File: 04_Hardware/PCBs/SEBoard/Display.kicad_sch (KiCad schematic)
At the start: 35 parts, among them IC3 PCA9306DCTT, IC4 TXS0102DCUR, J14 FH12S-30S-0.5SH_55_, J15 FH12-8S-0.5SH_55_, U1 SC200EEMNA-E53-UGNDA, U9 AP5724WG-7

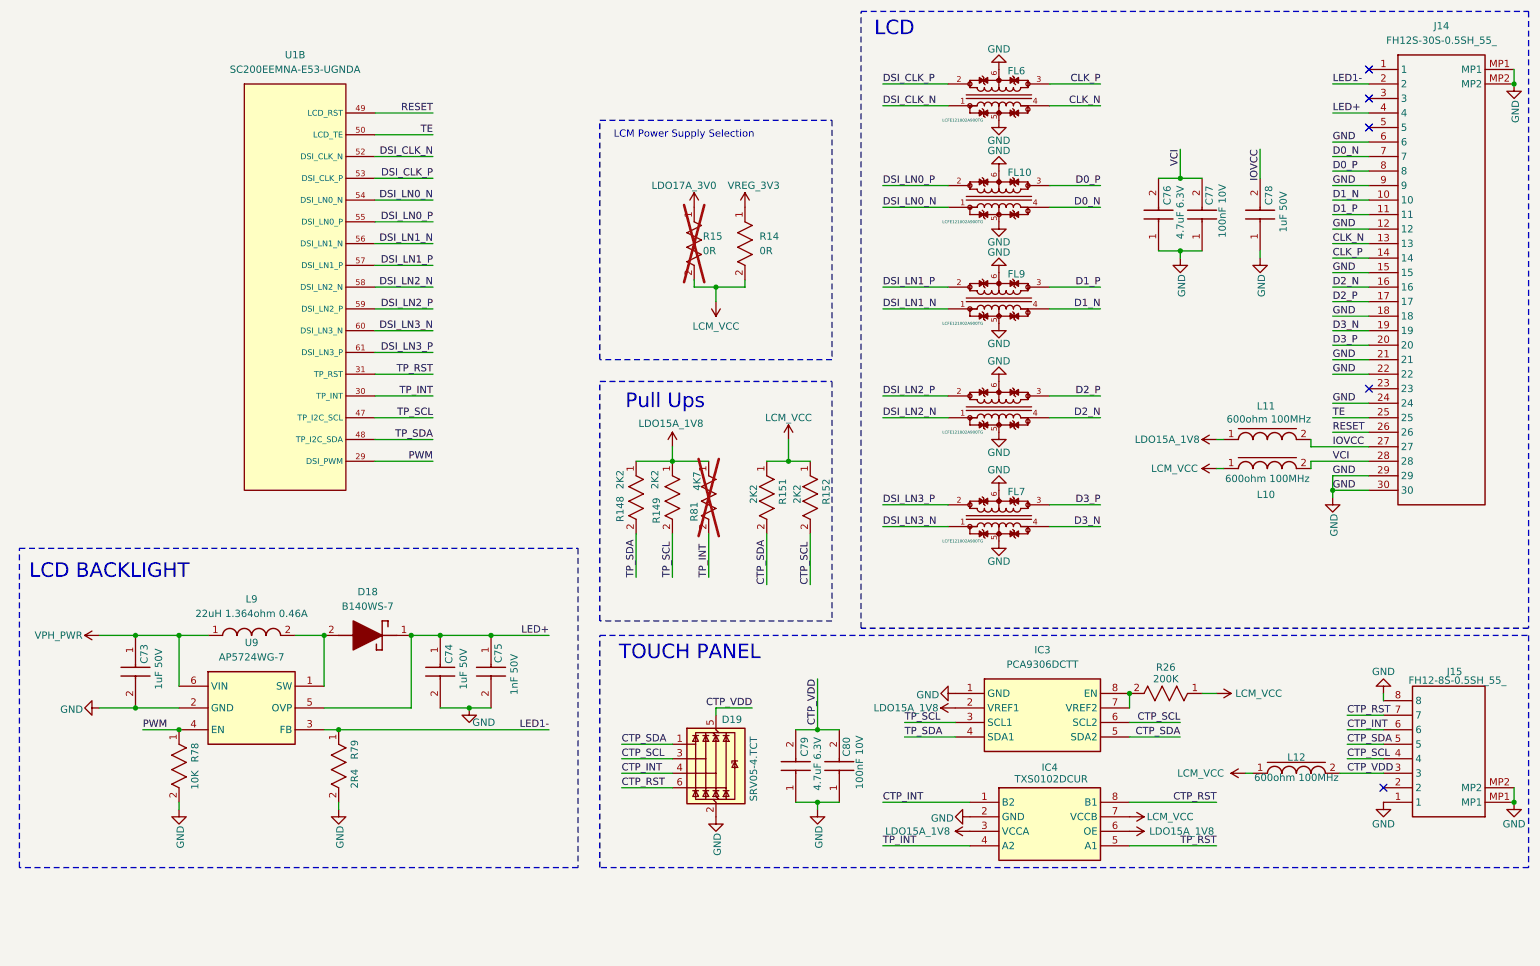
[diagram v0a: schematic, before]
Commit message: feat(schematic): add SE250B4 symbol to schematic (unchecked)
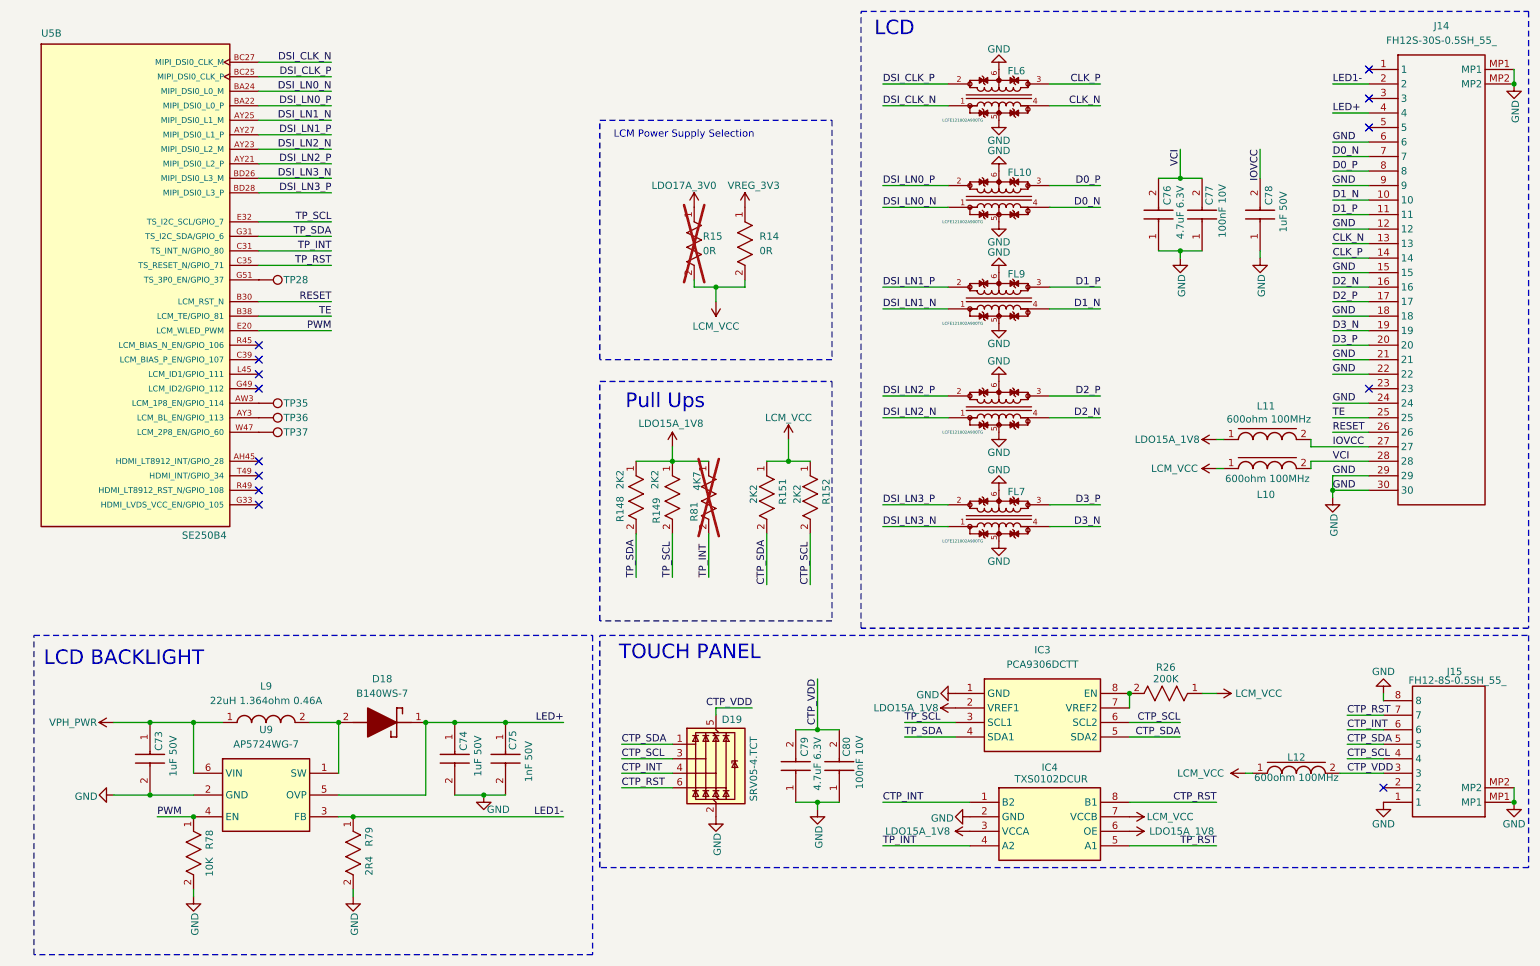
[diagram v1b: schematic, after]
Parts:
- removed U1: SC200EEMNA-E53-UGNDA, SEBoard:SC200E_SC206E, symbol SEBoard:SC200E
- added TP28, TP35, TP36, TP37: Sens_M, TestPoint:TestPoint_Pad_D1.0mm, symbol SEBoard:TestPoint
- added U5: SE250B4, 000MCLib:XCVR_SE250B4-NA, symbol 000MCLib:SE250B4
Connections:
- net DSI_CLK_N: now also U5.BC27 (MIPI_DSI0_CLK_M)
- net DSI_CLK_P: now also U5.BC25 (MIPI_DSI0_CLK_P)
- net DSI_LN0_N: now also U5.BA24 (MIPI_DSI0_L0_M)
- net DSI_LN0_P: now also U5.BA22 (MIPI_DSI0_L0_P)
- net DSI_LN1_N: now also U5.AY25 (MIPI_DSI0_L1_M)
- net DSI_LN1_P: now also U5.AY27 (MIPI_DSI0_L1_P)
- net DSI_LN2_N: now also U5.AY23 (MIPI_DSI0_L2_M)
- net DSI_LN2_P: now also U5.AY21 (MIPI_DSI0_L2_P)
- net DSI_LN3_N: now also U5.BD26 (MIPI_DSI0_L3_M)
- net DSI_LN3_P: now also U5.BD28 (MIPI_DSI0_L3_P)
- net PWM: now also U5.E20 (LCM_WLED_PWM)
- net RESET: now also U5.B30 (LCM_RST_N)
- net TE: now also U5.B38 (LCM_TE/GPIO_81)
- net TP_INT: now also U5.C31 (TS_INT_N/GPIO_80)
- net TP_RST: now also U5.C35 (TS_RESET_N/GPIO_71)
- net TP_SCL: now also U5.E32 (TS_I2C_SCL/GPIO_7)
- net TP_SDA: now also U5.G31 (TS_I2C_SDA/GPIO_6)
- new net: TP35.1, U5.AW3 (LCM_1P8_EN/GPIO_114)
- new net: TP36.1, U5.AY3 (LCM_BL_EN/GPIO_113)
- new net: TP28.1, U5.G51 (TS_3P0_EN/GPIO_37)
- new net: TP37.1, U5.W47 (LCM_2P8_EN/GPIO_60)
- no-connect marks 5 -> 13
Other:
- moved on the sheet: C73, C74, C75, D18, L9, R78, R79, U9

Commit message: feat: Updated schematic layout and moved new components to Layout
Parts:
- C73, C74, C78: footprint SEBoard:CAPC1005X55N -> 000MCLib:CAPC1005X55N; symbol SEBoard:GRM155R61H105KE05D -> 000MCLib:GRM155R61H105KE05D
- C75: footprint SEBoard:CAPC1005X55N -> 000MCLib:CAPC1005X55N; symbol SEBoard:GRM1555C1H102JA01D -> 000MCLib:GRM1555C1H102JA01D
- C76, C79: footprint SEBoard:CAPC1005X55N -> 000MCLib:CAPC1005X55N; symbol SEBoard:GRM155R60J475ME47D -> 000MCLib:GRM155R60J475ME47D
- C77, C80: footprint SEBoard:CAPC1005X55N -> 000MCLib:CAPC1005X55N; symbol SEBoard:GRM155R71A104KA01D -> 000MCLib:GRM155R71A104KA01D
- D18: footprint SEBoard:SOD2513X120N -> 000MCLib:SOD2513X120N; symbol SEBoard:B140WS-7 -> 000MCLib:B140WS-7
- D19: footprint SEBoard:SOT95P280X145-6N -> 000MCLib:SOT95P280X145-6N; symbol SEBoard:SRV05-4.TCT -> 000MCLib:SRV05-4.TCT
- FL10, FL6, FL7, FL8, FL9: footprint SEBoard:LCFE121002A900TG -> 000MCLib:LCFE121002A900TG; symbol SEBoard:LCFE121002A900TG -> 000MCLib:LCFE121002A900TG
- IC3: footprint SOP65P400X130-8N -> 000MCLib:SOP65P400X130-8N; symbol SEBoard:PCA9306DCTT -> 000MCLib:PCA9306DCTT
- IC4: footprint SEBoard:SOP50P310X90-8N -> 000MCLib:SOP50P310X90-8N; symbol SEBoard:TXS0102DCUR -> 000MCLib:TXS0102DCUR
- J14: footprint SEBoard:FH12S30S05SH55 -> 000MCLib:FH12S30S05SH55; symbol SEBoard:FH12S-30S-0.5SH_55_ -> 000MCLib:FH12S-30S-0.5SH_55_
- J15: footprint SEBoard:FH128S05SH55 -> 000MCLib:FH128S05SH55; symbol SEBoard:FH12-8S-0.5SH_55_ -> 000MCLib:FH12-8S-0.5SH_55_
- L10, L11, L12: footprint SEBoard:0402 -> 000MCLib:0402; symbol SEBoard:7427927291 -> 000MCLib:7427927291
- L9: footprint SEBoard:VLS2520 -> 000MCLib:VLS2520; symbol SEBoard:VLS252010CX-220M-1 -> 000MCLib:VLS252010CX-220M-1
- R14, R15: footprint SEBoard:RESC2012X50N -> 000MCLib:RESC2012X50N; symbol SEBoard:CRCW08050000Z0EA -> 000MCLib:CRCW08050000Z0EA
- R148, R149, R151, R152: footprint SEBoard:RC0402N_YAG -> 000MCLib:RC0402N_YAG; symbol SEBoard:RC0402JR-072K2L -> 000MCLib:RC0402JR-072K2L
- R26: footprint SEBoard:RC0402N_YAG -> 000MCLib:RC0402N_YAG; symbol SEBoard:RC0402FR-07200KL -> 000MCLib:RC0402FR-07200KL
- R78: footprint SEBoard:RC0402N_YAG -> 000MCLib:RC0402N_YAG; symbol SEBoard:RC0402JR-0710KL -> 000MCLib:RC0402JR-0710KL
- R79: footprint SEBoard:RC0402N_YAG -> 000MCLib:RC0402N_YAG; symbol SEBoard:RC0402JR-072R4L -> 000MCLib:RC0402JR-072R4L
- R81: footprint SEBoard:RC0402N_YAG -> 000MCLib:RC0402N_YAG; symbol SEBoard:RC0402JR-074K7L -> 000MCLib:RC0402JR-074K7L
- TP28, TP35, TP36, TP37: symbol SEBoard:TestPoint -> 000MCLib:TestPoint
- U9: footprint SEBoard:SOT95P285X140-6N -> 000MCLib:SOT95P285X140-6N; symbol SEBoard:AP5724WG-7 -> 000MCLib:AP5724WG-7

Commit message: feat: Updated schematic
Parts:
- added TP40: Sens_M, TestPoint:TestPoint_Pad_D1.0mm, symbol 000MCLib:TestPoint
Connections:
- net at U5.T49 (HDMI_INT/GPIO_34): now also TP40.1
- no-connect marks 13 -> 12
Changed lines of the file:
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@@
 	)
 	(no_connect
-		(at 57.15 96.52)
-	)
-	(no_connect
 		(at 254 151.13)
 	)
@@
 					(unit 1)
 				)
+			)
+		)
+	)
+	(symbol
+		(lib_id "000MCLib:TestPoint")
+		(at 57.15 96.52 270)
+		(unit 1)
+		(exclude_from_sim no)
+		(in_bom yes)
+		(on_board yes)
+		(dnp no)
+		(property "Reference" "TP40"
+			(at 61.468 96.52 90)
+			(effects
+				(font
+					(size 1.27 1.27)
+				)
+				(justify left)
+			)
+		)
+		(property "Value" "Sens_M"
+			(at 57.404 97.536 90)
+			(effects
+				(font
+					(size 0.635 0.635)
+				)
+				(hide yes)
+			)
+		)
+		(property "Footprint" "TestPoint:TestPoint_Pad_D1.0mm"
+			(at 57.15 101.6 0)
+			(effects
+				(font
+					(size 1.27 1.27)
+				)
+				(hide yes)
+			)
+		)
+		(property "Datasheet" "~"
+			(at 57.15 101.6 0)
+			(effects
+				(font
+					(size 1.27 1.27)
+				)
+				(hide yes)
+			)
+		)
+		(property "Description" "test point"
+			(at 57.15 96.52 0)
+			(effects
+				(font
+					(size 1.27 1.27)
+				)
+				(hide yes)
+			)
+		)
+		(pin "1"
+		)
+		(instances
+			(project "SEBoard"
+				(path "/38605b01-fdd9-41de-8a8b-501279ee3e8a/fd20983e-53dc-4079-9f17-527f4e836b8e"
+					(reference "TP40")
+					(unit 1)
+				)
